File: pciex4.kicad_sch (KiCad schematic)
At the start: 18 parts, among them J89 Bus_PCI_Express_x4

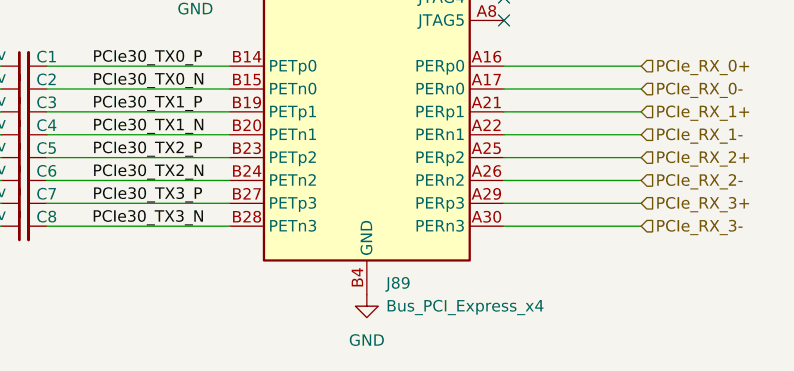
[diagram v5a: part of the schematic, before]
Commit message: Designators in PSU restored
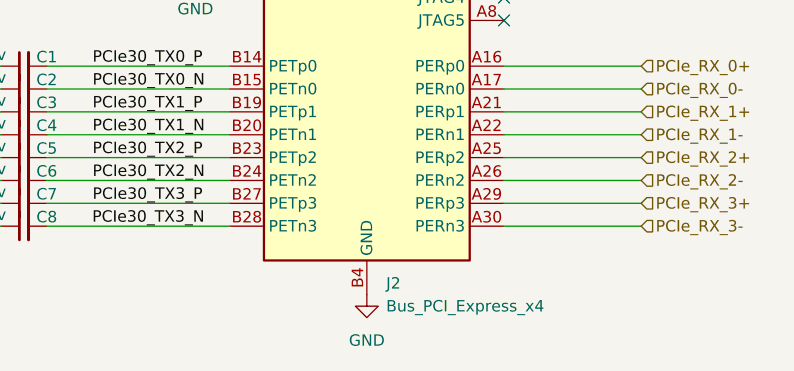
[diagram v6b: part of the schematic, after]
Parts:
- renumbered J89 to J2
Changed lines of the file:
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@@
 		(dnp no)
 		(fields_autoplaced yes)
-		(property "Reference" "J89"
+		(property "Reference" "J2"
 			(at 212.9633 182.88 0)
 			(show_name no)
@@
 			(project "Carrier_Board"
 				(path "/e768274e-12f3-4f83-96f6-abb7638e0bc1/d05d8b94-71f3-437a-a0af-11ed4e3069d0"
-					(reference "J89")
+					(reference "J2")
 					(unit 1)
 				)
